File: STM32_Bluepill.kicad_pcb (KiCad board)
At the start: 2 copper layers, 0 parts

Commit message: Layout: Add Rat's Nest and edit page info
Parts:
- added C1: 10u, Capacitor_SMD:C_0603_1608Metric, F.Cu at (149.9, 96.5)
- added C10: 10p, Capacitor_SMD:C_0402_1005Metric, F.Cu at (149.3, 105.2)
- added C11: 10p, Capacitor_SMD:C_0402_1005Metric, F.Cu at (146.9, 109.2)
- added C12: 22u, Capacitor_SMD:C_0805_2012Metric, F.Cu at (140.7, 102.4)
- added C13: 22u, Capacitor_SMD:C_0805_2012Metric, F.Cu at (140.7, 105.4)
- added C2: 100n, Capacitor_SMD:C_0402_1005Metric, F.Cu at (149.3, 107.2)
- added C3: 100n, Capacitor_SMD:C_0402_1005Metric, F.Cu at (155.0, 103.3)
- added C4: 100n, Capacitor_SMD:C_0402_1005Metric, F.Cu at (158.0, 99.8)
- added C5: 100n, Capacitor_SMD:C_0402_1005Metric, F.Cu at (152.2, 103.3)
- added C6: 10n, Capacitor_SMD:C_0402_1005Metric, F.Cu at (152.2, 105.2)
- added C7: 1u, Capacitor_SMD:C_0402_1005Metric, F.Cu at (149.3, 103.3)
- added C8: 1u, Capacitor_SMD:C_0402_1005Metric, F.Cu at (149.8, 109.2)
- added C9: 100n, Capacitor_SMD:C_0402_1005Metric, F.Cu at (155.1, 99.8)
- added D1: RED, LED_SMD:LED_0603_1608Metric, F.Cu at (140.6, 108.8)
- added FB1: 120R, Inductor_SMD:L_0603_1608Metric, F.Cu at (149.9, 99.0)
- added J1: USB_B_Micro, Connector_USB:USB_Micro-B_Wuerth_629105150521, F.Cu at (133.0, 104.8)
- added J2: Conn_01x04_Male, Connector_PinHeader_2.54mm:PinHeader_1x04_P2.54mm_Vertical, F.Cu at (145.5, 97.6)
- added J3: Conn_01x04_Male, Connector_PinHeader_2.54mm:PinHeader_1x04_P2.54mm_Vertical, F.Cu at (145.5, 85.3)
- added J4: Conn_01x04_Male, Connector_PinHeader_2.54mm:PinHeader_1x04_P2.54mm_Vertical, F.Cu at (150.2, 85.3)
- added R1: 10k, Resistor_SMD:R_0402_1005Metric, F.Cu at (159.2, 95.4)
- added R2: 1k5, Resistor_SMD:R_0402_1005Metric, F.Cu at (165.3, 92.3)
- added R3: 1k5, Resistor_SMD:R_0402_1005Metric, F.Cu at (152.2, 101.3)
- added R4: 1k5, Resistor_SMD:R_0402_1005Metric, F.Cu at (144.0, 108.5)
- added R5: 1k5, Resistor_SMD:R_0402_1005Metric, F.Cu at (149.3, 101.3)
- added SW_BOOT1: SW_SPDT, Button_Switch_THT:SW_E-Switch_EG1224_SPDT_Angled, F.Cu at (131.4, 86.6)
- added U1: STM32F103C8T6, Package_QFP:LQFP-48_7x7mm_P0.5mm, F.Cu at (158.2, 88.7)
- added U2: AMS1117-3.3, Package_TO_SOT_SMD:SOT-223-3_TabPin2, F.Cu at (168.8, 87.1)
- added Y1: 16MHz, Crystal:Crystal_SMD_3225-4Pin_3.2x2.5mm, F.Cu at (155.1, 96.6)

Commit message: Begin routing by importing rat's nest
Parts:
- moved C10 83.9 mm to (233.2, 107.8)
- moved C11 83.9 mm to (230.8, 111.8)
- moved C2 83.9 mm to (233.2, 109.8)
- moved C3 83.9 mm to (238.9, 105.8)
- moved C4 83.9 mm to (241.9, 102.4)
- moved C5 83.9 mm to (236.1, 105.8)
- moved C6 83.9 mm to (236.1, 107.8)
- moved C7 83.9 mm to (233.2, 105.8)
- moved C8 83.9 mm to (233.7, 111.8)
- moved D1 83.9 mm to (224.5, 111.4)
- moved J1 83.9 mm to (216.9, 107.3)
- moved J2 83.9 mm to (229.4, 100.2)
- moved J3 83.9 mm to (229.4, 87.9)
- moved J4 83.9 mm to (234.1, 87.9)
- moved R1 83.9 mm to (243.1, 98.0)
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
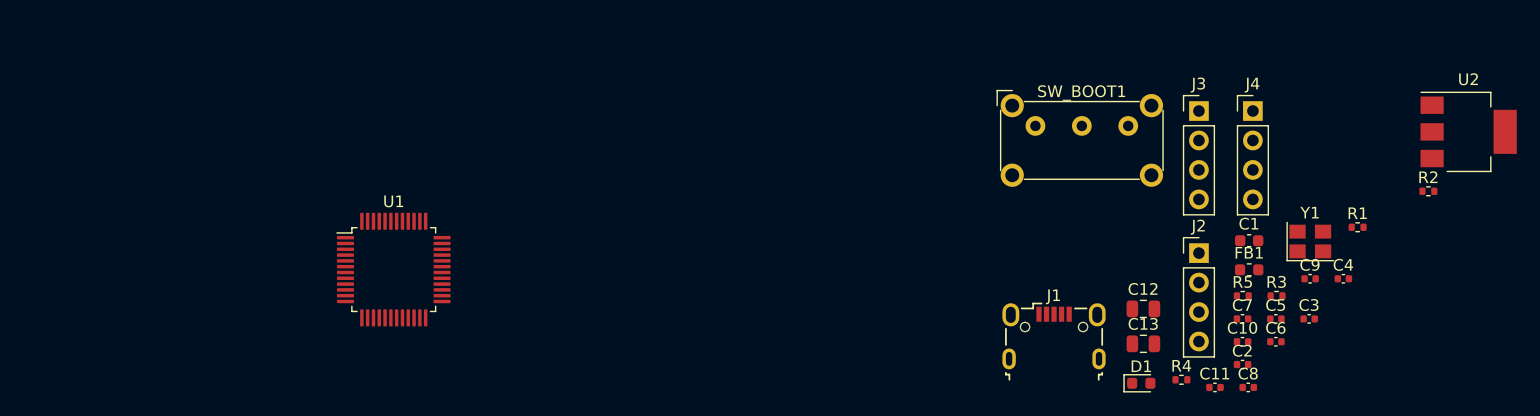
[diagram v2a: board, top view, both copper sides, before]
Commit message: Layout: Layout decoupling caps, filtering, and oscillator
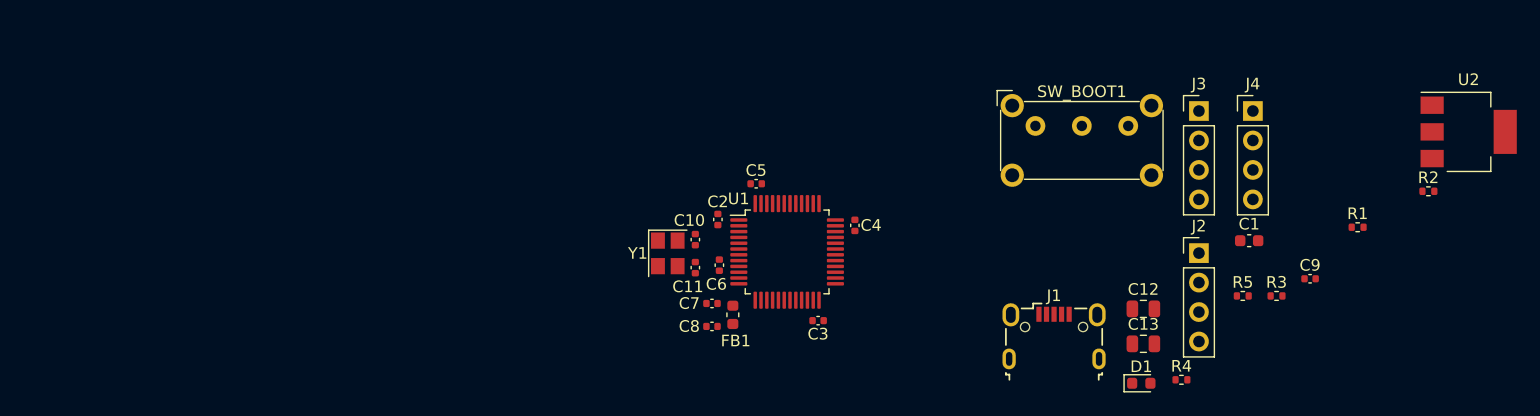
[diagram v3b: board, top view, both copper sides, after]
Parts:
- moved Y1 55.4 mm to (183.6, 100.2), turned to -90 degrees
- moved C6 48.4 mm to (188.1, 101.2), turned to 90 degrees
- moved C10 48.0 mm to (186.0, 99.0), turned to 90 degrees
- moved C2 46.9 mm to (188.0, 97.3), turned to 90 degrees
- moved C8 46.5 mm to (187.5, 106.5), turned to 180 degrees
- moved C5 46.3 mm to (191.3, 94.2)
- moved C11 46.0 mm to (186.0, 101.4), turned to 90 degrees
- moved C7 45.8 mm to (187.5, 104.5), turned to 180 degrees
- moved FB1 44.7 mm to (189.2, 105.5), turned to -90 degrees
- moved C4 42.4 mm to (199.8, 97.8), turned to -90 degrees
- moved C3 42.3 mm to (196.6, 106.0), turned to 180 degrees
- moved U1 33.9 mm to (193.9, 100.1)

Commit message: Layout: Place USB and SWD (Serial Wirte Debugger)
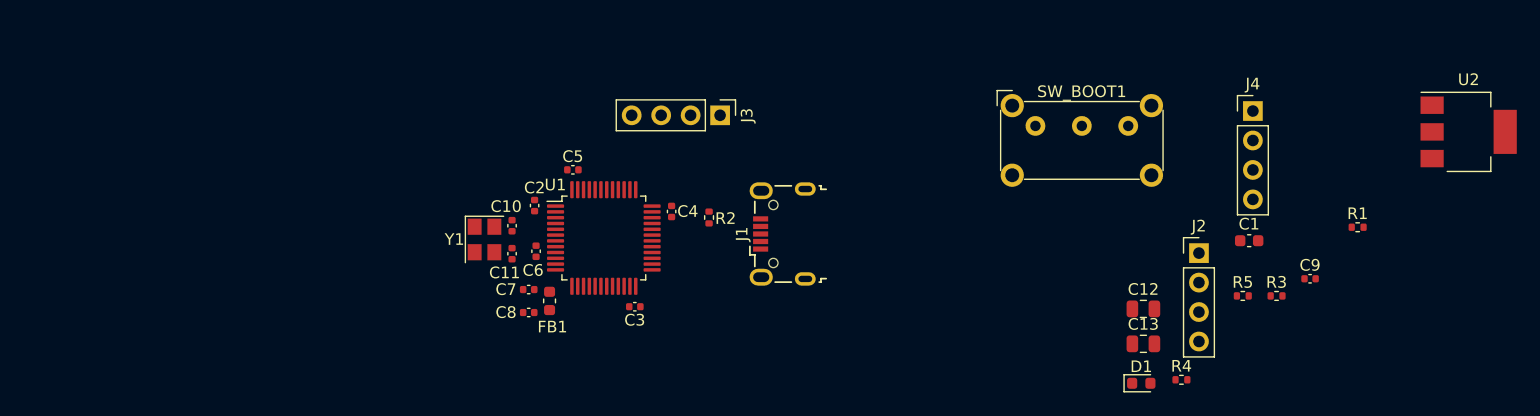
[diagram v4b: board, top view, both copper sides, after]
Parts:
- moved R2 62.1 mm to (187.2, 97.1), turned to -90 degrees
- moved J3 41.3 mm to (188.2, 88.3), turned to -90 degrees
- moved J1 25.0 mm to (193.5, 98.5), turned to 90 degrees
- moved C2 15.8 mm to (172.2, 96.1)
- moved C5 15.8 mm to (175.5, 93.0)
- moved C7 15.8 mm to (171.7, 103.3)
- moved C8 15.8 mm to (171.7, 105.3)
- moved FB1 15.8 mm to (173.4, 104.3)
- moved U1 15.8 mm to (178.1, 98.9)
- moved C10 15.8 mm to (170.2, 97.8)
- moved C11 15.8 mm to (170.2, 100.2)
- moved C3 15.8 mm to (180.8, 104.8)
- moved C4 15.8 mm to (184.0, 96.6)
- moved Y1 15.8 mm to (167.8, 99.0)
- moved C6 15.8 mm to (172.3, 100.0)

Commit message: Layout: Change switch's footprint to be a smaller SMD one
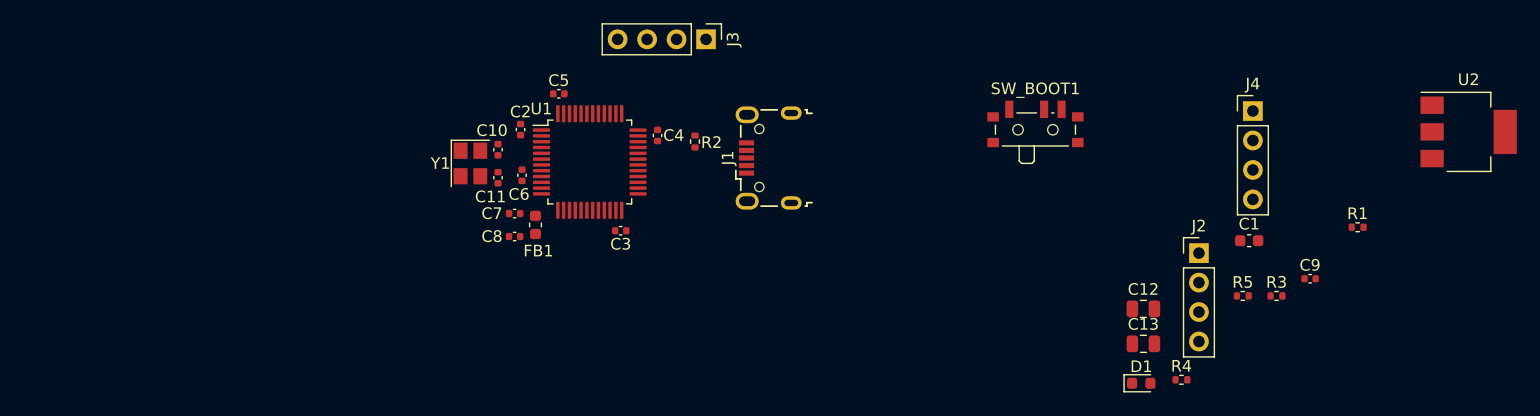
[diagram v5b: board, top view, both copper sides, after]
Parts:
- SW_BOOT1: footprint Button_Switch_THT:SW_E-Switch_EG1224_SPDT_Angled -> Button_Switch_SMD:SW_SPDT_PCM12
- moved C6 6.66 mm to (171.1, 93.5)
- moved U1 6.66 mm to (176.9, 92.3)
- moved C10 6.66 mm to (169.0, 91.3)
- moved C11 6.66 mm to (169.0, 93.7)
- moved C3 6.66 mm to (179.6, 98.2)
- moved C4 6.66 mm to (182.8, 90.0)
- moved J3 6.66 mm to (186.9, 81.8)
- moved Y1 6.66 mm to (166.6, 92.5)
- moved C2 6.66 mm to (170.9, 89.5)
- moved C5 6.66 mm to (174.2, 86.5)
- moved C7 6.66 mm to (170.4, 96.8)
- moved C8 6.66 mm to (170.4, 98.8)
- moved FB1 6.66 mm to (172.2, 97.8)
- moved J1 6.66 mm to (192.3, 92.0)
- moved R2 6.66 mm to (186.0, 90.6)
